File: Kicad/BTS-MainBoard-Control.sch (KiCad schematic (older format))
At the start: 24 parts, among them J3 Molex Micro Lock (1.25mm 1.5A), J4 Conn_01x14, U1 HIP4080A

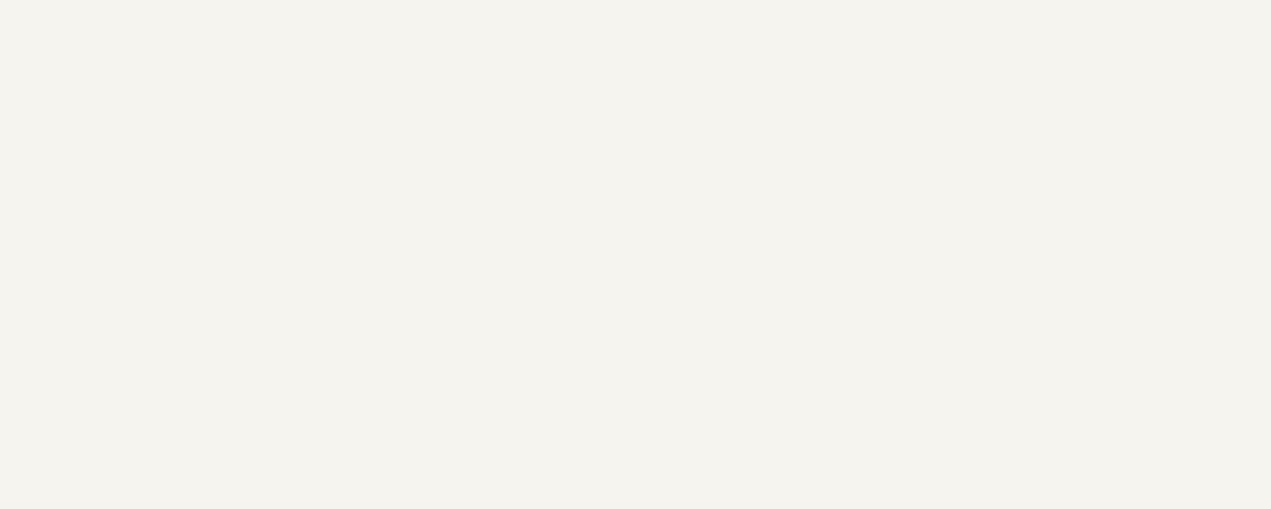
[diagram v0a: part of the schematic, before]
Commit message: Moved Libraries folder and renamed project files
Signed-off-by: bebenlebricolo <benoittarrade@hotmail.fr>
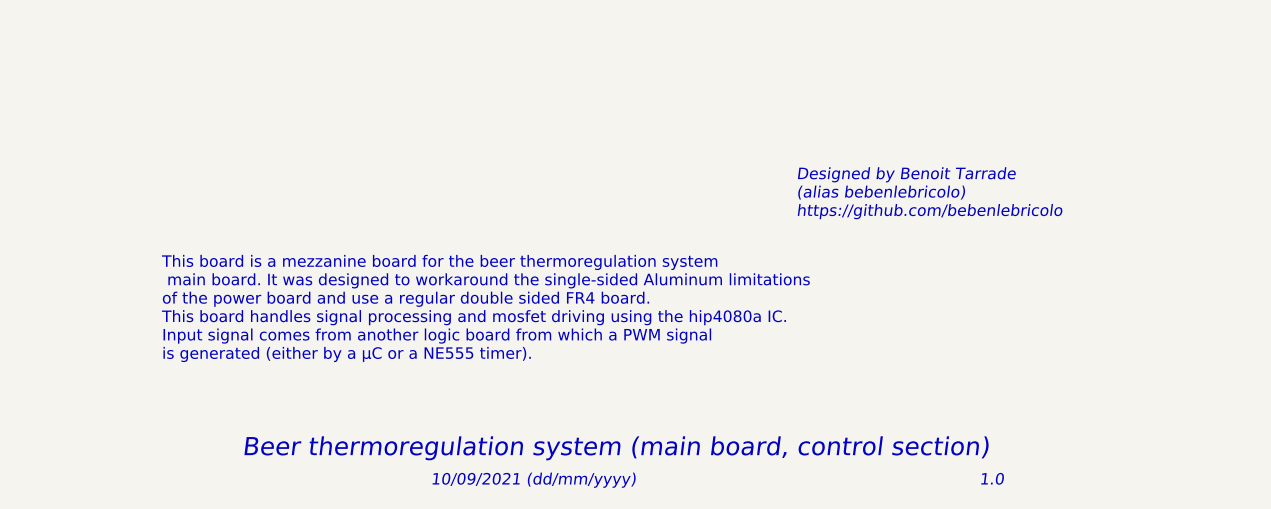
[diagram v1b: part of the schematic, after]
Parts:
- J3: footprint PeltierSwitchingMainBoard_control:Molex_MicroLock_1.25_01x06 -> BTS-MainBoard-Control:Molex_MicroLock_1.25_01x06
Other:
- note added: "1.0"
- note added: "10/09/2021 (dd/mm/yyyy)"
- note added: "Beer thermoregulation system (main board, control section)"
- note added: "Designed by Benoit Tarrade\n(alias bebenlebricolo)\nhttps://github.com/bebenlebricolo"
- note added: "This board is a mezzanine board for the beer thermoregulation system\n main board. It was designed to workaround the single-sided Aluminum limitations\nof the power board and use a regular double sided FR4 board.\nThis board handles signal processing and mosfet driving using the hip4080a IC.\nInput signal comes from another logic board from which a PWM signal \nis generated (either by a µC or a N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"
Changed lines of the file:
@@
 F 0 "J3" H 2530 6392 50  0000 L CNN
 F 1 "Molex Micro Lock (1.25mm 1.5A)" H 2530 6301 50  0000 L CNN
-F 2 "PeltierSwitchingMainBoard_control:Molex_MicroLock_1.25_01x06" H 2450 6400 50  0001 C CNN
+F 2 "BTS-MainBoard-Control:Molex_MicroLock_1.25_01x06" H 2450 6400 50  0001 C CNN
 F 3 "~" H 2450 6400 50  0001 C CNN
 	1    2450 6400
@@
 Text Label 6500 2900 2    50   ~ 0
 Vcc
+Text Notes 7350 7500 0    79   Italic 0
+Beer thermoregulation system (main board, control section)
+Text Notes 10575 7625 0    50   Italic 0
+1.0
+Text Notes 8175 7625 0    50   Italic 0
+10/09/2021 (dd/mm/yyyy)
+Text Notes 7000 7075 0    50   ~ 0
+This board is a mezzanine board for the beer thermoregulation system\n main board. It was designed to workaround the single-sided Aluminum limitations\nof the power board and use a regular double sided FR4 board.\nThis board handles signal processing and mosfet driving using the hip4080a IC.\nInput signal comes from another logic board from which a PWM signal \nis generated (either by a µC or a NE555 timer).
+Text Notes 9775 6450 0    50   Italic 0
+Designed by Benoit Tarrade\n(alias bebenlebricolo)\nhttps://github.com/bebenlebricolo
 $EndSCHEMATC

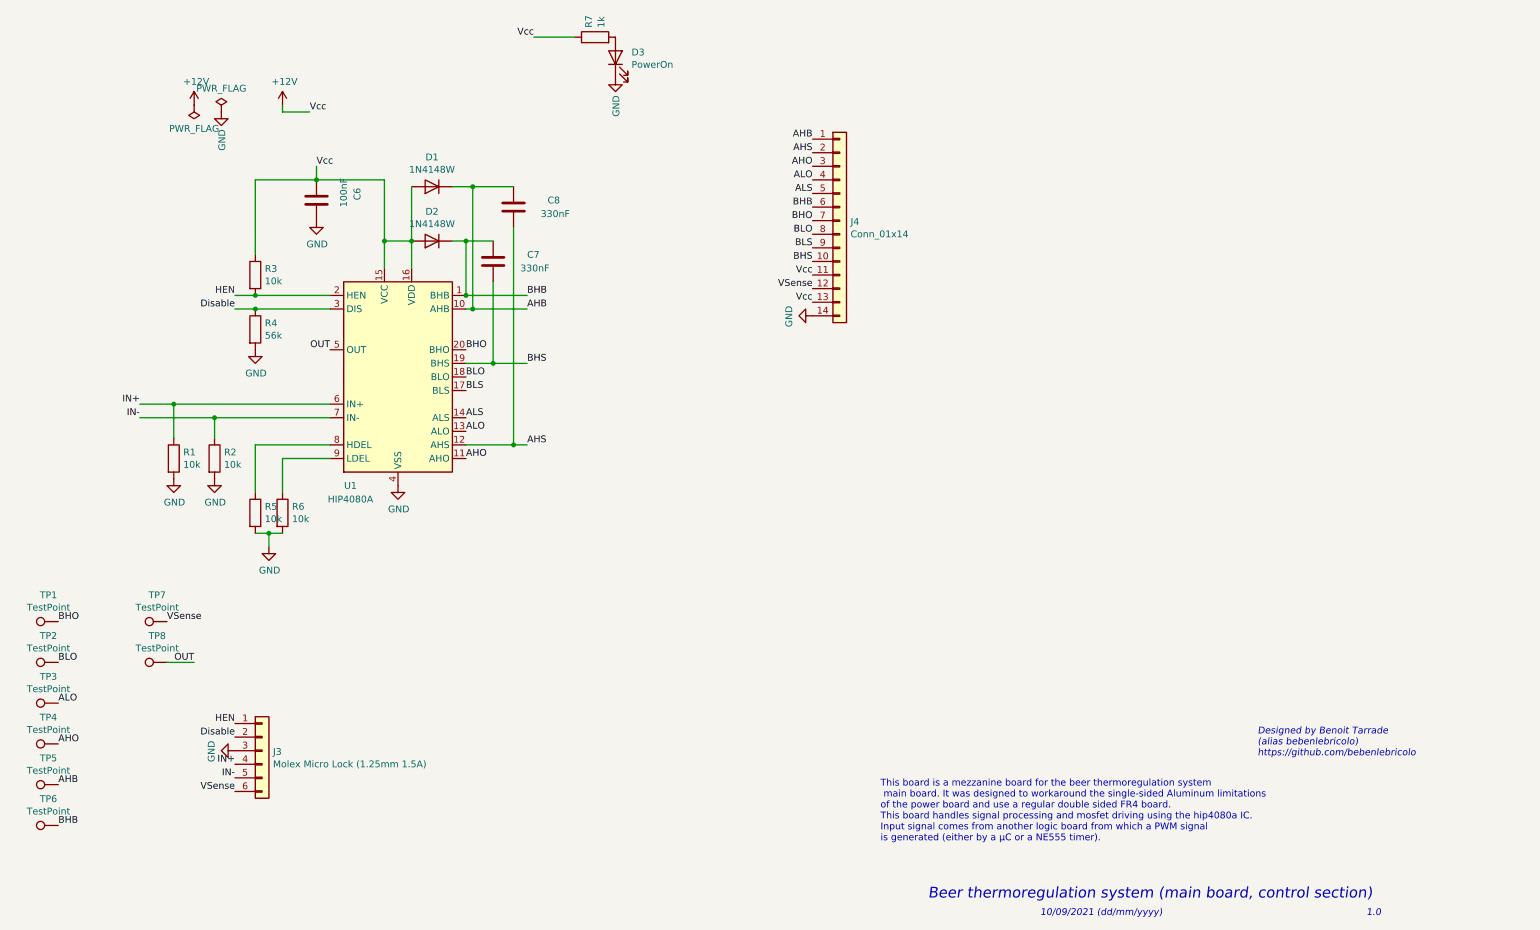
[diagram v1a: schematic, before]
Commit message: Added power mosfet to drive cooling fans
Signed-off-by: bebenlebricolo <benoittarrade@hotmail.fr>
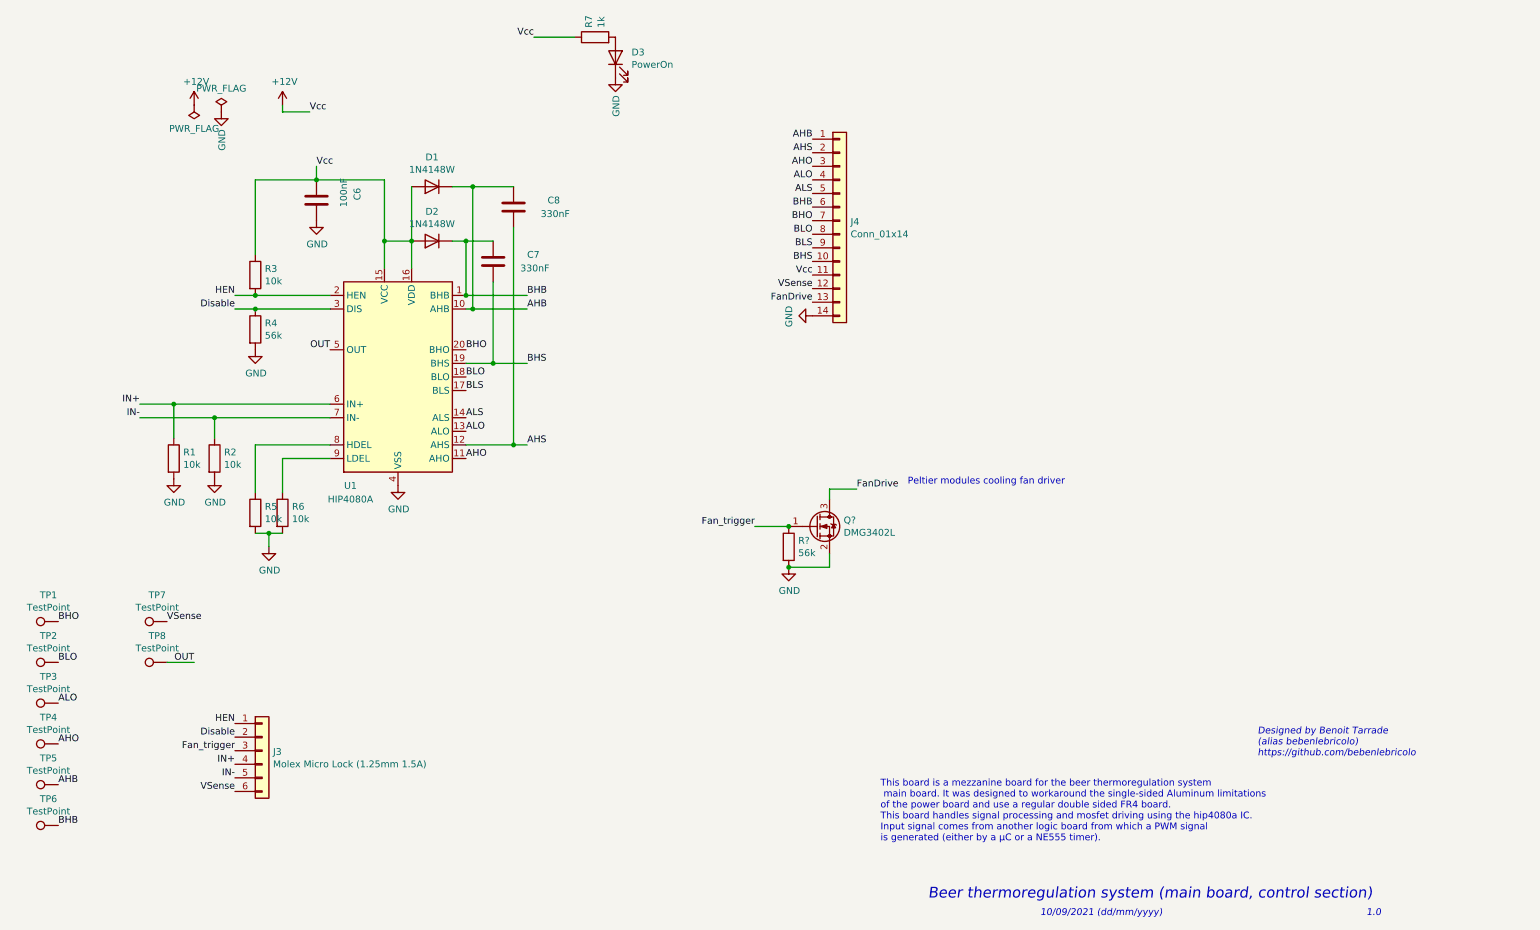
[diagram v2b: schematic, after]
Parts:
- added Q?: DMG3402L, Package_TO_SOT_SMD:SOT-23, symbol Transistor_FET:DMG3402L
- added R?: 56k, Resistor_SMD:R_1206_3216Metric_Pad1.30x1.75mm_HandSolder, symbol Device:R
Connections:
- net +12V: no longer J4.13 (Pin_13)
- net GND: now also Q?.2 (S), R?.2; no longer J3.3 (Pin_3)
- new net FanDrive: J4.13 (Pin_13), Q?.3 (D)
- new net Fan_trigger: J3.3 (Pin_3), Q?.1 (G), R?.1
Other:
- note added: "Peltier modules cooling fan driver"
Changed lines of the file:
@@
 	1    0    0    -1
-$EndComp
-$Comp
-L power:GND #PWR0103
-U 1 1 6141E90C
-P 2250 6400
-F 0 "#PWR0103" H 2250 6150 50  0001 C CNN
-F 1 "GND" H 2255 6227 50  0000 C CNN
-F 2 "" H 2250 6400 50  0001 C CNN
-F 3 "" H 2250 6400 50  0001 C CNN
-	1    2250 6400
-	0    1    1    0
 $EndComp
 Text Label 6500 2500 2    50   ~ 0
@@
 Text Label 6500 2300 2    50   ~ 0
 ALS
-Text Label 6500 3100 2    50   ~ 0
-Vcc
 $Comp
 L power:GND #PWR013
@@
 Text Notes 9775 6450 0    50   Italic 0
 Designed by Benoit Tarrade\n(alias bebenlebricolo)\nhttps://github.com/bebenlebricolo
+Text Label 2250 6400 2    50   ~ 0
+Fan_trigger
+$Comp
+L power:GND #PWR?
+U 1 1 613DFDA4
+P 6325 5050
+F 0 "#PWR?" H 6325 4800 50  0001 C CNN
+F 1 "GND" H 6330 4877 50  0000 C CNN
+F 2 "" H 6325 5050 50  0001 C CNN
+F 3 "" H 6325 5050 50  0001 C CNN
+	1    6325 5050
+	1    0    0    -1
+$EndComp
+Wire Wire Line
+	6325 5050 6625 5050
+Wire Wire Line
+	6625 5050 6625 4950
+Wire Wire Line
+	6325 4750 6075 4750
+$Comp
+L Device:R R?
+U 1 1 613E252B
+P 6325 4900
+F 0 "R?" H 6395 4946 50  0000 L CNN
+F 1 "56k" H 6395 4855 50  0000 L CNN
+F 2 "Resistor_SMD:R_1206_3216Metric_Pad1.30x1.75mm_HandSolder" V 6255 4900 50  0001 C CNN
+F 3 "~" H 6325 4900 50  0001 C CNN
+	1    6325 4900
+	1    0    0    -1
+$EndComp
+Connection ~ 6325 5050
+Wire Wire Line
+	6625 4550 6625 4475
+Wire Wire Line
+	6625 4475 6825 4475
+Text Label 6075 4750 2    50   ~ 0
+Fan_trigger
+Text Notes 7200 4450 0    50   ~ 0
+Peltier modules cooling fan driver
+$Comp
+L Transistor_FET:DMG3402L Q?
+U 1 1 613EE4C5
+P 6525 4750
+F 0 "Q?" H 6729 4796 50  0000 L CNN
+F 1 "DMG3402L" H 6729 4705 50  0000 L CNN
+F 2 "Package_TO_SOT_SMD:SOT-23" H 6725 4675 50  0001 L CIN
+F 3 "http://www.diodes.com/assets/Datasheets/DMG3402L.pdf" H 6525 4750 50  0001 L CNN
+	1    6525 4750
+	1    0    0    -1
+$EndComp
+Connection ~ 6325 4750
+Text Label 6825 4475 0    50   ~ 0
+FanDrive
+Text Label 6500 3100 2    50   ~ 0
+FanDrive
 $EndSCHEMATC

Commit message: Replotted gerbers and updated silkscreen
Signed-off-by: bebenlebricolo <benoittarrade@hotmail.fr>
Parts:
- gave numbers to parts that had none: 2
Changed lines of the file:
@@
 Fan_trigger
 $Comp
-L power:GND #PWR?
+L power:GND #PWR01
 U 1 1 613DFDA4
 P 6325 5050
-F 0 "#PWR?" H 6325 4800 50  0001 C CNN
+F 0 "#PWR01" H 6325 4800 50  0001 C CNN
 F 1 "GND" H 6330 4877 50  0000 C CNN
 F 2 "" H 6325 5050 50  0001 C CNN
@@
 	6325 4750 6075 4750
 $Comp
-L Device:R R?
+L Device:R R8
 U 1 1 613E252B
 P 6325 4900
-F 0 "R?" H 6395 4946 50  0000 L CNN
+F 0 "R8" H 6395 4946 50  0000 L CNN
 F 1 "56k" H 6395 4855 50  0000 L CNN
 F 2 "Resistor_SMD:R_1206_3216Metric_Pad1.30x1.75mm_HandSolder" V 6255 4900 50  0001 C CNN
@@
 Peltier modules cooling fan driver
 $Comp
-L Transistor_FET:DMG3402L Q?
+L Transistor_FET:DMG3402L Q1
 U 1 1 613EE4C5
 P 6525 4750
-F 0 "Q?" H 6729 4796 50  0000 L CNN
+F 0 "Q1" H 6729 4796 50  0000 L CNN
 F 1 "DMG3402L" H 6729 4705 50  0000 L CNN
 F 2 "Package_TO_SOT_SMD:SOT-23" H 6725 4675 50  0001 L CIN

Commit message: Created BOM
Signed-off-by: bebenlebricolo <benoittarrade@hotmail.fr>
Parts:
- J3: value Molex Micro Lock (1.25mm 1.5A) -> Input Signals Connector
- J4: value Conn_01x14 -> Out connector
- Q1: value DMG3402L -> DMG3418L-7
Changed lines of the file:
@@
 P 2450 6400
 F 0 "J3" H 2530 6392 50  0000 L CNN
-F 1 "Molex Micro Lock (1.25mm 1.5A)" H 2530 6301 50  0000 L CNN
+F 1 "Input Signals Connector" H 2530 6301 50  0000 L CNN
 F 2 "BTS-MainBoard-Control:Molex_MicroLock_1.25_01x06" H 2450 6400 50  0001 C CNN
 F 3 "~" H 2450 6400 50  0001 C CNN
@@
 P 6700 2500
 F 0 "J4" H 6780 2492 50  0000 L CNN
-F 1 "Conn_01x14" H 6780 2401 50  0000 L CNN
+F 1 "Out connector" H 6780 2401 50  0000 L CNN
 F 2 "Connector_PinHeader_2.54mm:PinHeader_1x14_P2.54mm_Vertical" H 6700 2500 50  0001 C CNN
 F 3 "~" H 6700 2500 50  0001 C CNN
@@
 P 6525 4750
 F 0 "Q1" H 6729 4796 50  0000 L CNN
-F 1 "DMG3402L" H 6729 4705 50  0000 L CNN
+F 1 "DMG3418L-7" H 6729 4705 50  0000 L CNN
 F 2 "Package_TO_SOT_SMD:SOT-23" H 6725 4675 50  0001 L CIN
 F 3 "http://www.diodes.com/assets/Datasheets/DMG3402L.pdf" H 6525 4750 50  0001 L CNN
